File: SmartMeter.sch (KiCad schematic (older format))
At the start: 20 parts, among them J1 RJ12, Q1 BC547, Q2 BC547, SW1 SW_Push, U1 WeMos_mini, U2 TLC555CP

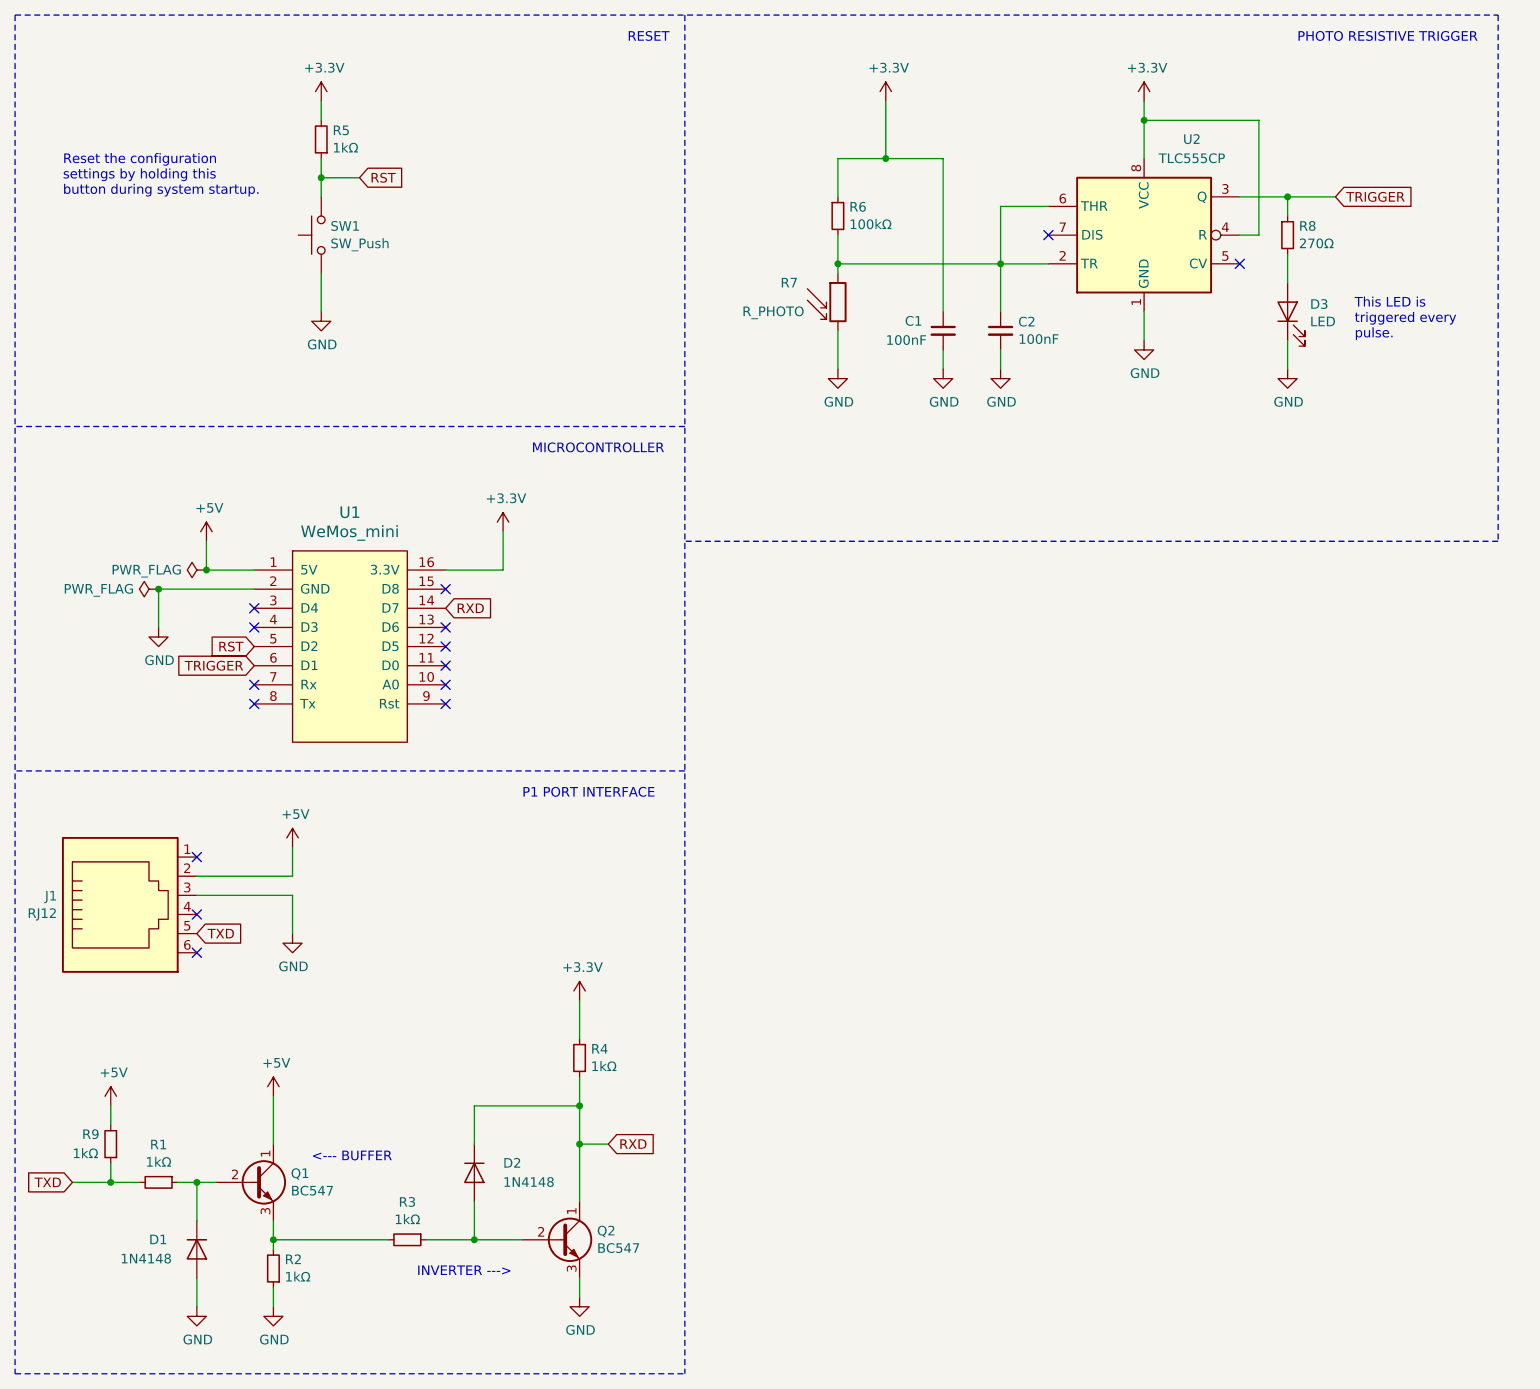
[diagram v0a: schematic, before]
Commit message: hardware: update schematics + PCB to version 2.0
Update the schematics and layout to v2.0. The pulse counter using a
TLC555 has been removed, together with the LDR and blue status LED. An
RGB (common anode) status LED has been added to the board.

Signed-off-by: Michel Megens <dev@bietje.net>
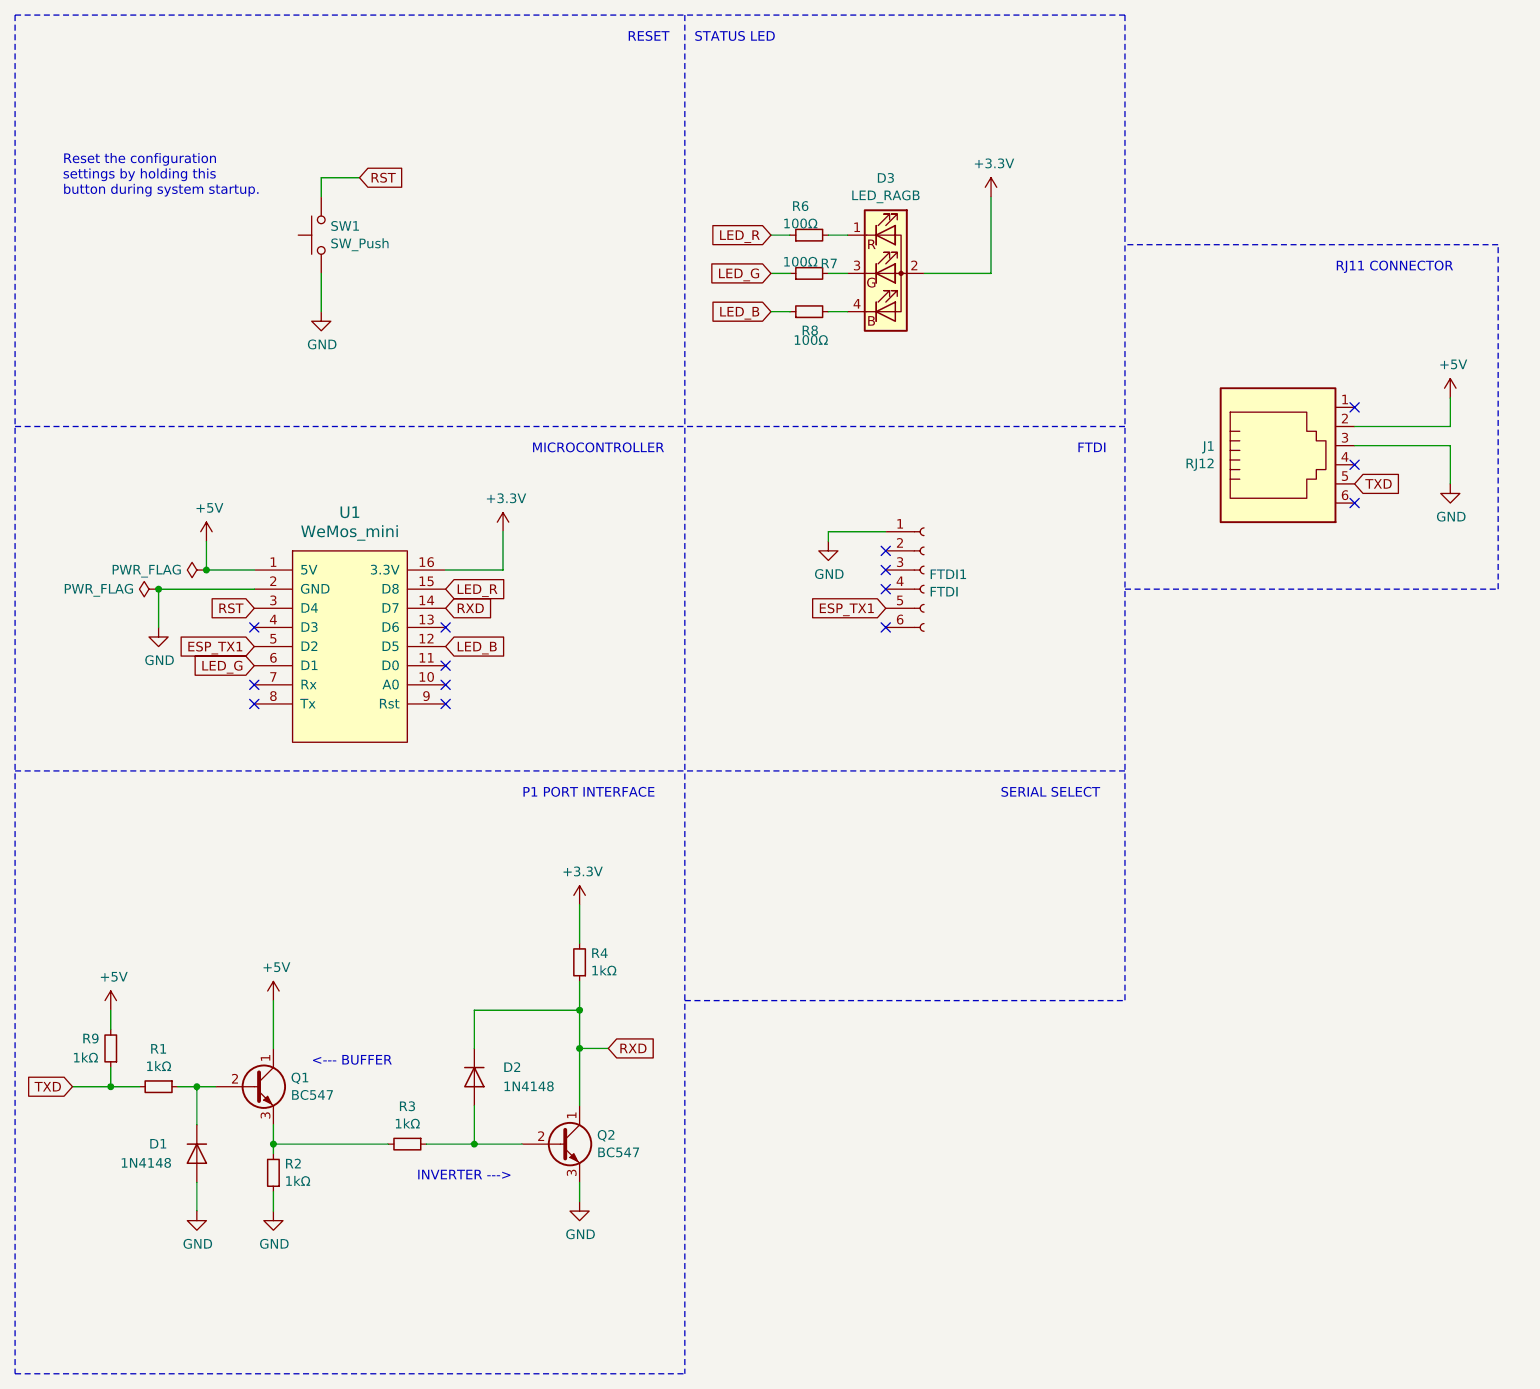
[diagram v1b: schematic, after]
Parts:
- removed C1, C2: 100nF, Capacitor_THT:C_Disc_D5.0mm_W2.5mm_P2.50mm, symbol Device:C_Small
- removed D3: LED, LED_THT:LED_D5.0mm, symbol Device:LED
- removed R5: 1kΩ, Resistor_THT:R_Axial_DIN0309_L9.0mm_D3.2mm_P12.70mm_Horizontal, symbol Device:R_Small
- removed R7: R_PHOTO, OptoDevice:R_LDR_7x6mm_P5.1mm_Vertical, symbol Device:R_PHOTO
- removed U2: TLC555CP, Package_DIP:DIP-8_W7.62mm, symbol Timer:TLC555CP
- added D3: LED_RAGB, LED_THT:LED_D5.0mm-4_RGB_Wide_Pins, symbol Device:LED_RAGB
- added FTDI1: FTDI, Connector_PinHeader_2.54mm:PinHeader_1x06_P2.54mm_Vertical, symbol Connector:Conn_01x06_Female
- added R7: 100Ω, Resistor_THT:R_Axial_DIN0309_L9.0mm_D3.2mm_P12.70mm_Horizontal, symbol Device:R_Small
- Q1, Q2: footprint Package_TO_SOT_THT:TO-92_Inline -> Package_TO_SOT_THT:TO-92_Wide
- R6: value 100kΩ -> 100Ω
- R8: value 270Ω -> 100Ω
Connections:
- net +3V3: now also D3.2 (A); no longer R6.1
- net GND: now also FTDI1.1 (Pin_1)
- net RST: now also U1.3 (D4); no longer U1.5 (D2)
- net at R6.2: now also D3.1 (RK)
- net at R8.2: now also D3.4 (BK)
- net LED_B: now reaches U1.12 (D5)
- net LED_B: now also R8.1
- net LED_R: now reaches U1.15 (D8)
- net LED_R: now also R6.1
- net TRIGGER renamed LED_G
- net LED_G: now also R7.1; no longer R8.1
- new net: D3.3 (GK), R7.2
- new net ESP_TX1: FTDI1.5 (Pin_5), U1.5 (D2)
- no-connect marks 15 -> 14
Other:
- note added: "FTDI"
- note added: "RJ11 CONNECTOR"
- note added: "SERIAL SELECT"
- note added: "STATUS LED"
- note removed: "PHOTO RESISTIVE TRIGGER"
- note removed: "This LED is\ntriggered every\npulse."
- moved on the sheet: D1, D2, J1, Q1, Q2, R1, R2, R3, R4, R9
